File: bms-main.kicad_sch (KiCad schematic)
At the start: 1 part, among them U1 STM32C542CCU6

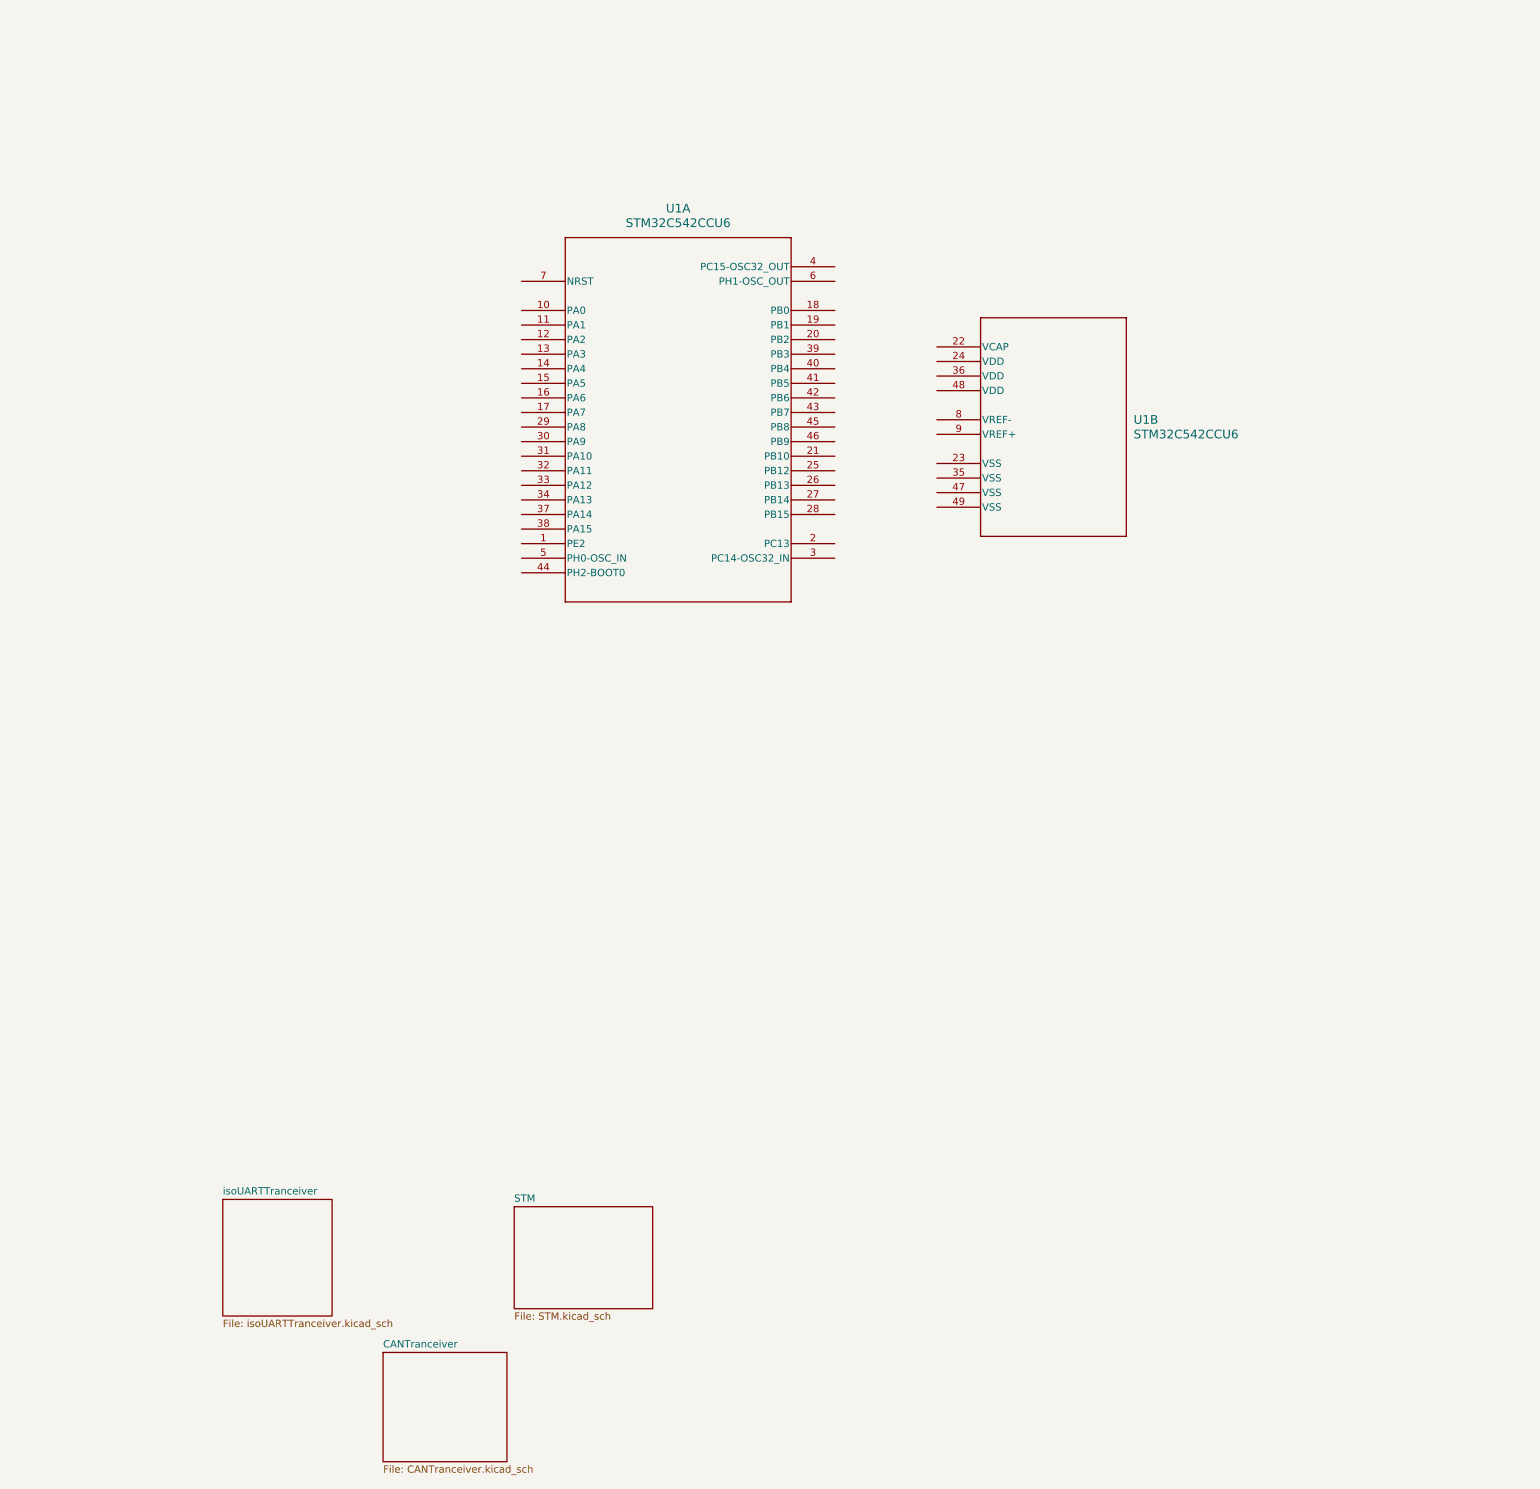
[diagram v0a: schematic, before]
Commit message: added stm pins
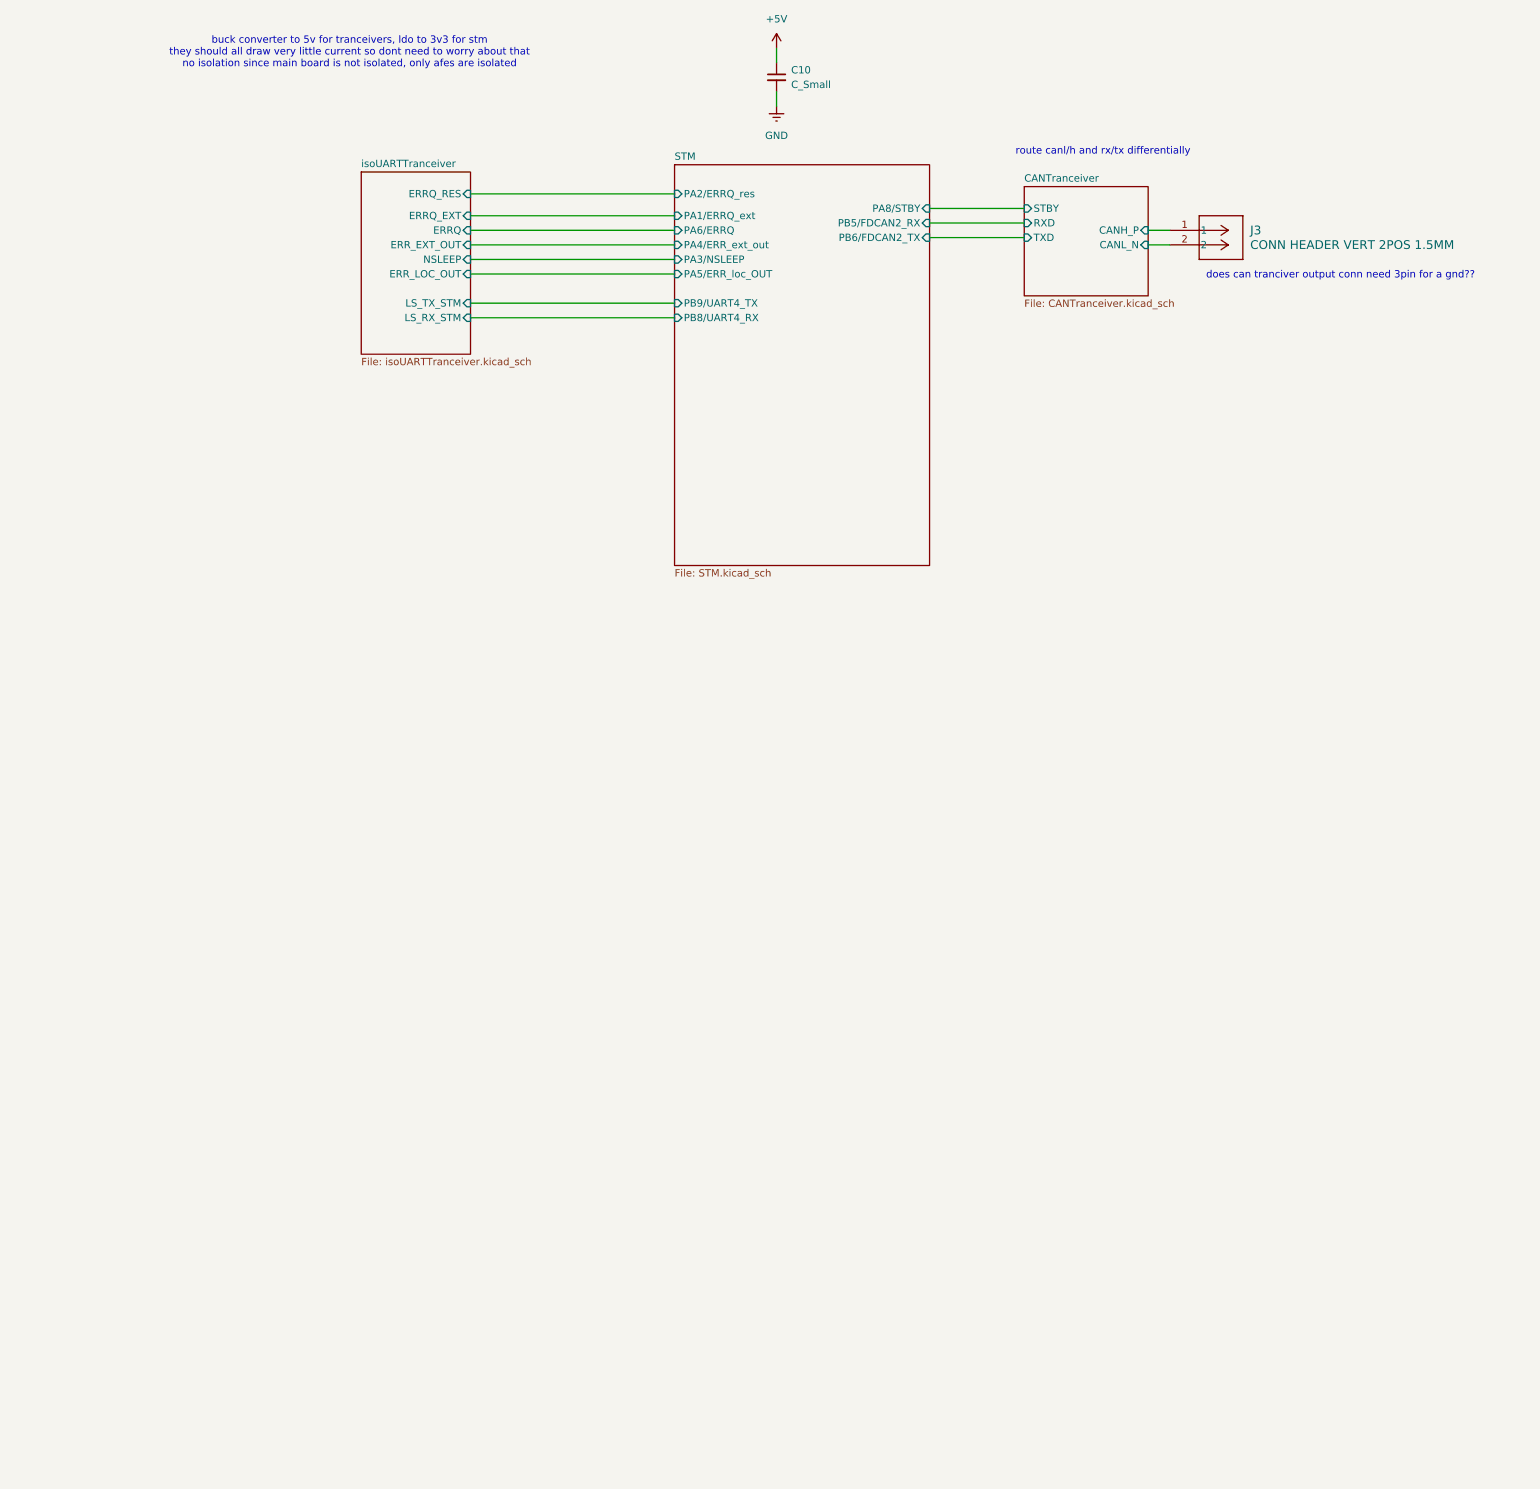
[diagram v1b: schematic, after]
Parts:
- removed U1: STM32C542CCU6, footprints:UFQFPN-48_STM, symbol symbols:STM32C542CCU6
- added C10: C_Small, symbol Device:C_Small
- added J3: CONN HEADER VERT 2POS 1.5MM, footprints:CONN_B2B-ZR_02P_JST, symbol symbols:B2B-ZR
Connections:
- new net +5V: C10.1
- new net CANTranceiver/CANH_P: J3.1
- new net CANTranceiver/CANL_N: J3.2
- new net GND: C10.2
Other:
- sheet CANTranceiver ports: added CANH_P, CANL_N, RXD, STBY, TXD; removed none
- sheet STM ports: added PA1/ERRQ_ext, PA2/ERRQ_res, PA3/NSLEEP, PA4/ERR_ext_out, PA5/ERR_loc_OUT, PA6/ERRQ, PA8/STBY, PB5/FDCAN2_RX, PB6/FDCAN2_TX, PB8/UART4_RX, PB9/UART4_TX; removed none
- sheet isoUARTTranceiver ports: added ERRQ, ERRQ_EXT, ERRQ_RES, ERR_EXT_OUT, ERR_LOC_OUT, LS_RX_STM, LS_TX_STM, NSLEEP; removed none
- note added: "buck converter to 5v for tranceivers, ldo to 3v3 for stm they should all draw very little current so dont need to worry about that no isolation since main board is not isolated, only afes are isolated"
- note added: "does can tranciver output conn need 3pin for a gnd??"
- note added: "route canl/h and rx/tx differentially"

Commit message: finished can and power
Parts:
- removed C10: C_Small, symbol Device:C_Small
- removed J3: CONN HEADER VERT 2POS 1.5MM, footprints:CONN_B2B-ZR_02P_JST, symbol symbols:B2B-ZR
- added J1, J4, J5: CONN HEADER VERT 2POS 1.5MM, footprints:CONN_B2B-ZR_02P_JST, symbol symbols:B2B-ZR
- added J3: XT60PW-M, footprints:AMASS_XT60PW-M, symbol symbols:XT60PW-M
- added J6: CONN HEADER VERT 4POS 2.5MM, footprints:CONN_B4B-XH-A_JST, symbol symbols:B4B-XH-A
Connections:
- net CANTranceiver/CANH_P: now also J6.2
- net CANTranceiver/CANL_N: now also J6.3
- net GND: now also J3.2 (N), J3.SH1 (SHIELD), J3.SH2 (SHIELD), J4.2, J5.2, J6.4
- new net 3V3: J5.1
- new net 48V: J3.1 (P)
- new net 5V: J4.1
- new net isoUARTTranceiver/IFH_H: J1.1
- new net isoUARTTranceiver/IFH_L: J1.2
- no-connect marks 0 -> 1
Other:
- sheet isoUARTTranceiver ports: added IFH_H, IFH_L; removed none
- note added: "AFE 1"
- note added: "Power from PD Board"
- note removed: "buck converter to 5v for tranceivers, ldo to 3v3 for stm they should all draw very little current so dont need to worry about that no isolation since main board is not isolated, only afes are isolated"
- note removed: "does can tranciver output conn need 3pin for a gnd??"

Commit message: schematic done
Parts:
- removed J3: XT60PW-M, footprints:AMASS_XT60PW-M, symbol symbols:XT60PW-M
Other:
- added sheet CurrentSense (CurrentSense.kicad_sch)
- sheet STM ports: added PB0/ADC1_IN6; removed none
- moved on the sheet: J4, J5

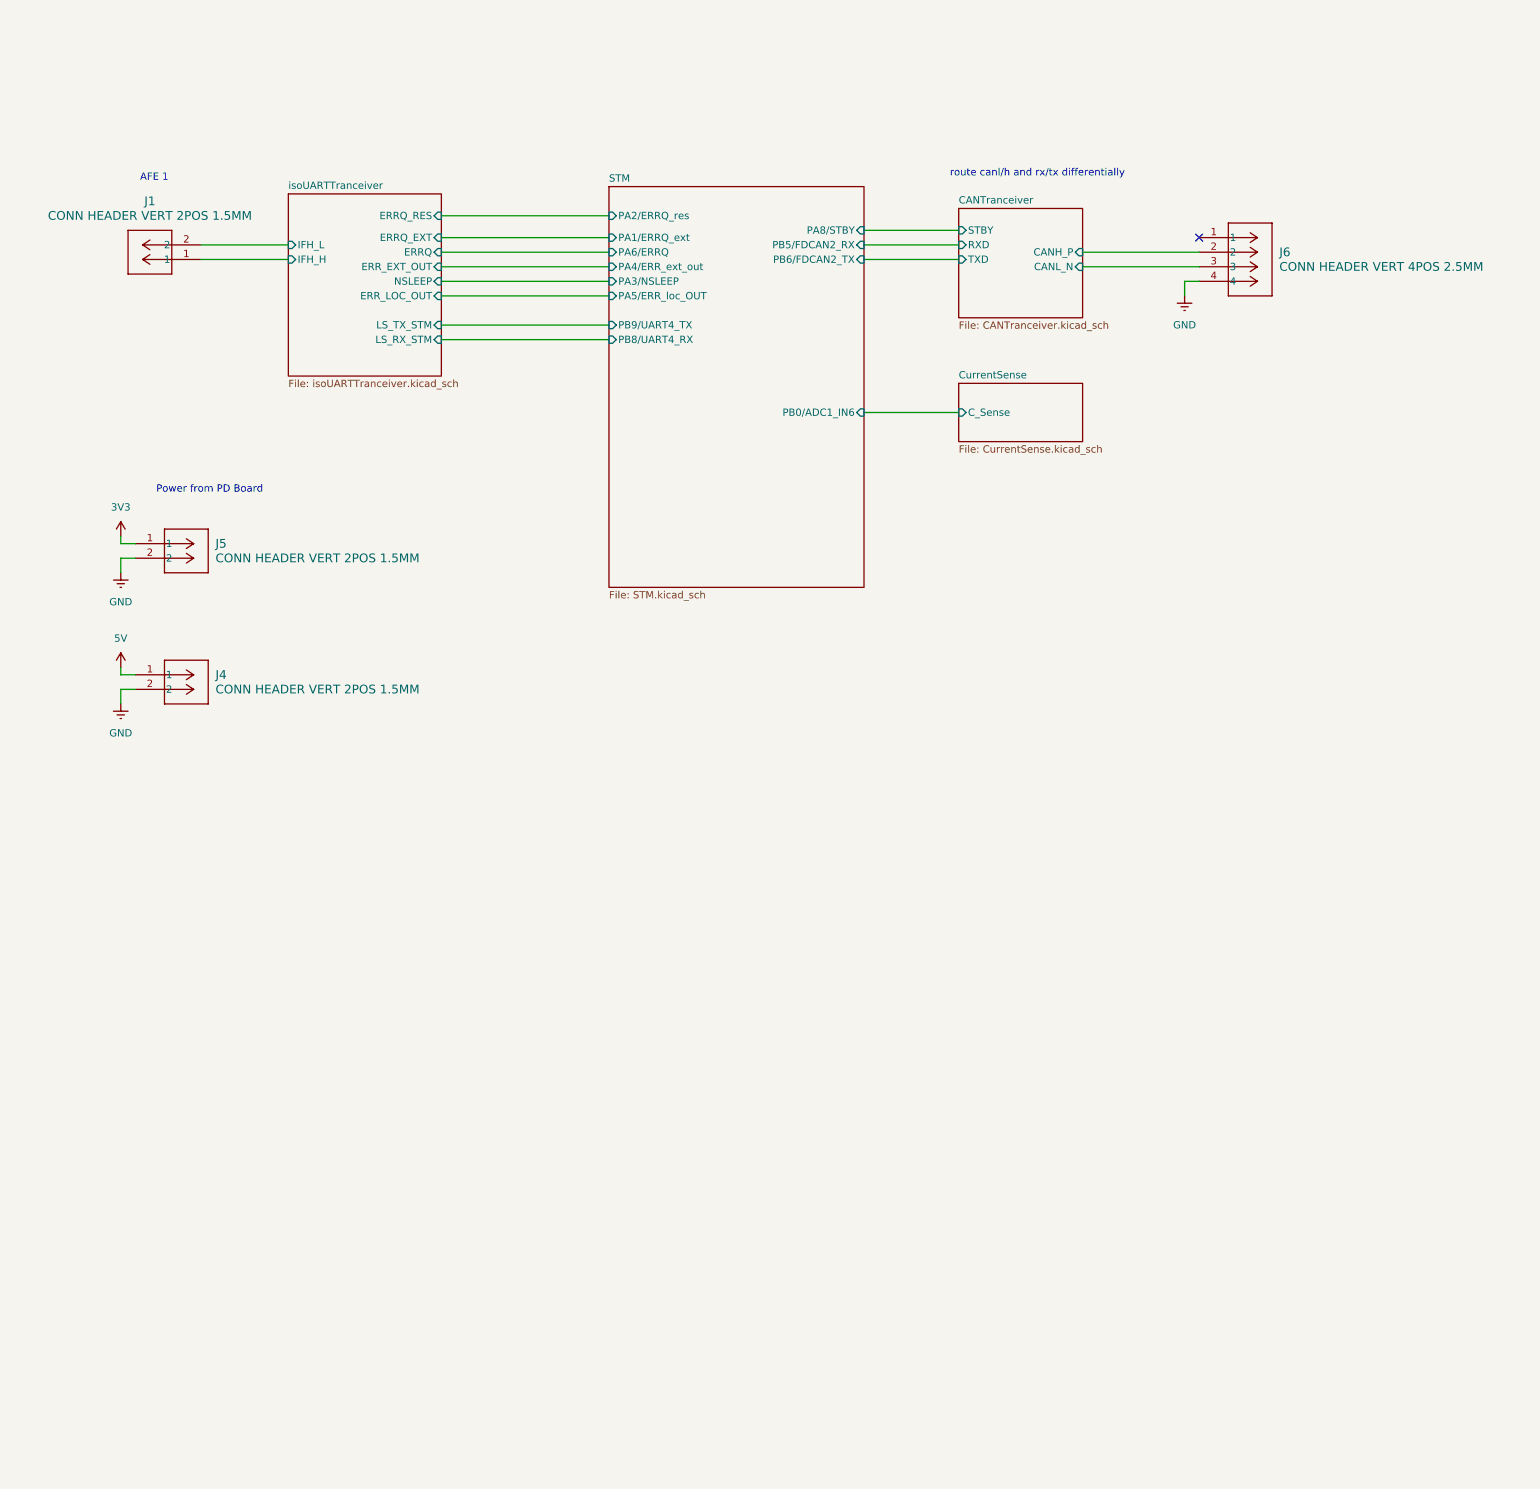
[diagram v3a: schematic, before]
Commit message: cleaned up schematic
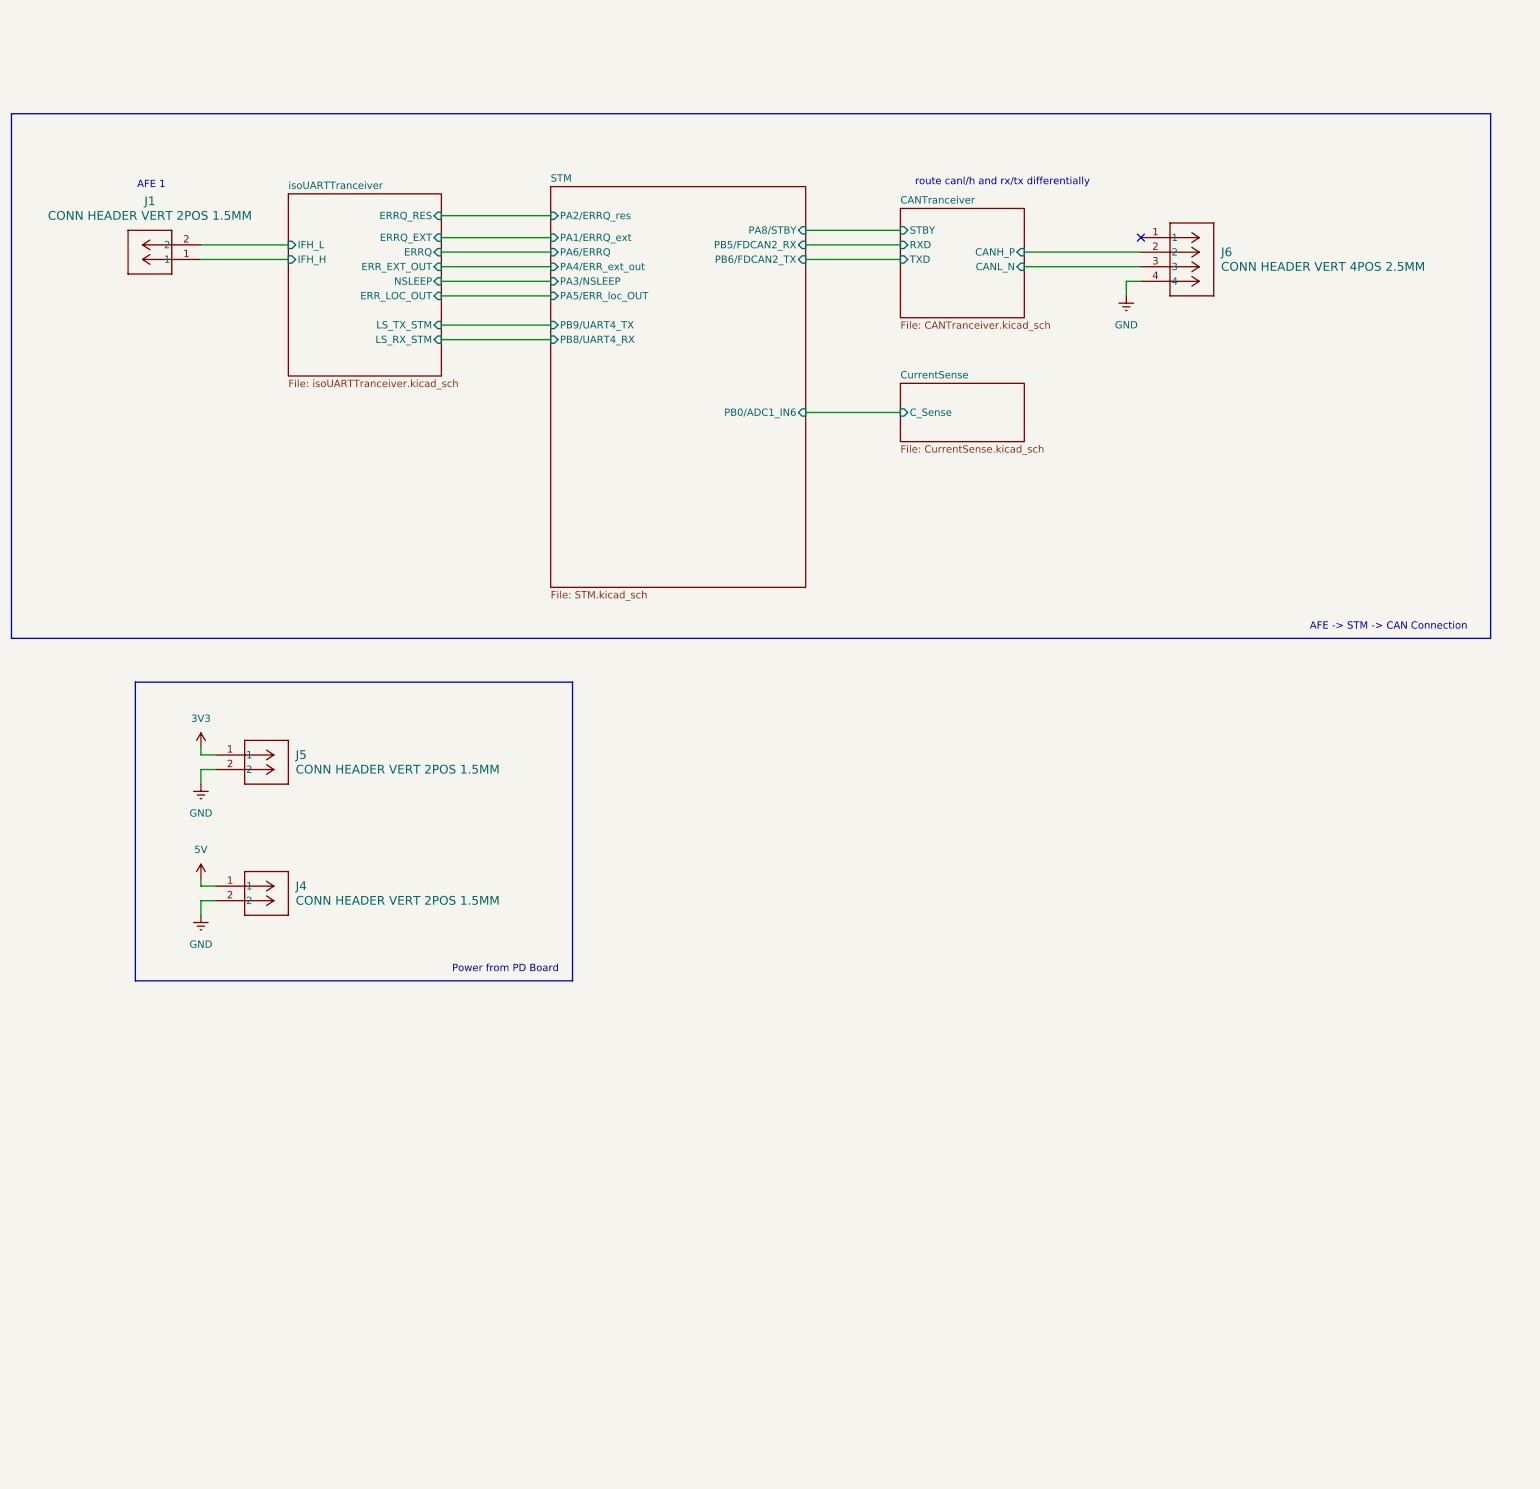
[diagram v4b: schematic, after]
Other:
- note added: "AFE -> STM -> CAN Connection"
- moved on the sheet: J4, J5, J6

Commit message: minor changes
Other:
- sheet STM ports: added PA0/ADC1_IN5, PA11/CAN1_RX, PA12/CAN1_TX, PA7/STBY, PB10/UART3_TX, PB11/UART4_RX; removed PA8/STBY, PB0/ADC1_IN6, PB5/FDCAN2_RX, PB6/FDCAN2_TX, PB8/UART4_RX, PB9/UART4_TX
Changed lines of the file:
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@@
 			)
 		)
-		(pin "PB9{slash}UART4_TX" input
+		(pin "PB10{slash}UART3_TX" input
 			(at 111.76 71.12 180)
 			(effects
@@
 			)
 		)
-		(pin "PB8{slash}UART4_RX" input
+		(pin "PB11{slash}UART4_RX" input
 			(at 111.76 73.66 180)
 			(effects
@@
 			)
 		)
-		(pin "PA8{slash}STBY" input
+		(pin "PA7{slash}STBY" input
 			(at 156.21 54.61 0)
 			(effects
@@
 			)
 		)
-		(pin "PB6{slash}FDCAN2_TX" input
+		(pin "PA12{slash}CAN1_TX" input
 			(at 156.21 59.69 0)
 			(effects
@@
 			)
 		)
-		(pin "PB5{slash}FDCAN2_RX" input
+		(pin "PA11{slash}CAN1_RX" input
 			(at 156.21 57.15 0)
 			(effects
@@
 			)
 		)
-		(pin "PB0{slash}ADC1_IN6" input
+		(pin "PA0{slash}ADC1_IN5" input
 			(at 156.21 86.36 0)
 			(effects
